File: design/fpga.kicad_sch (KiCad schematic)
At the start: 80 parts, among them J7 DEBUG_FPGA_GPIO, J8 DIGILENT_JTAG_HS2_01X06, SW1 RST, SW2 PROG, U13 XC7S15-FTGB196, U14 IS25LP064A-JKx

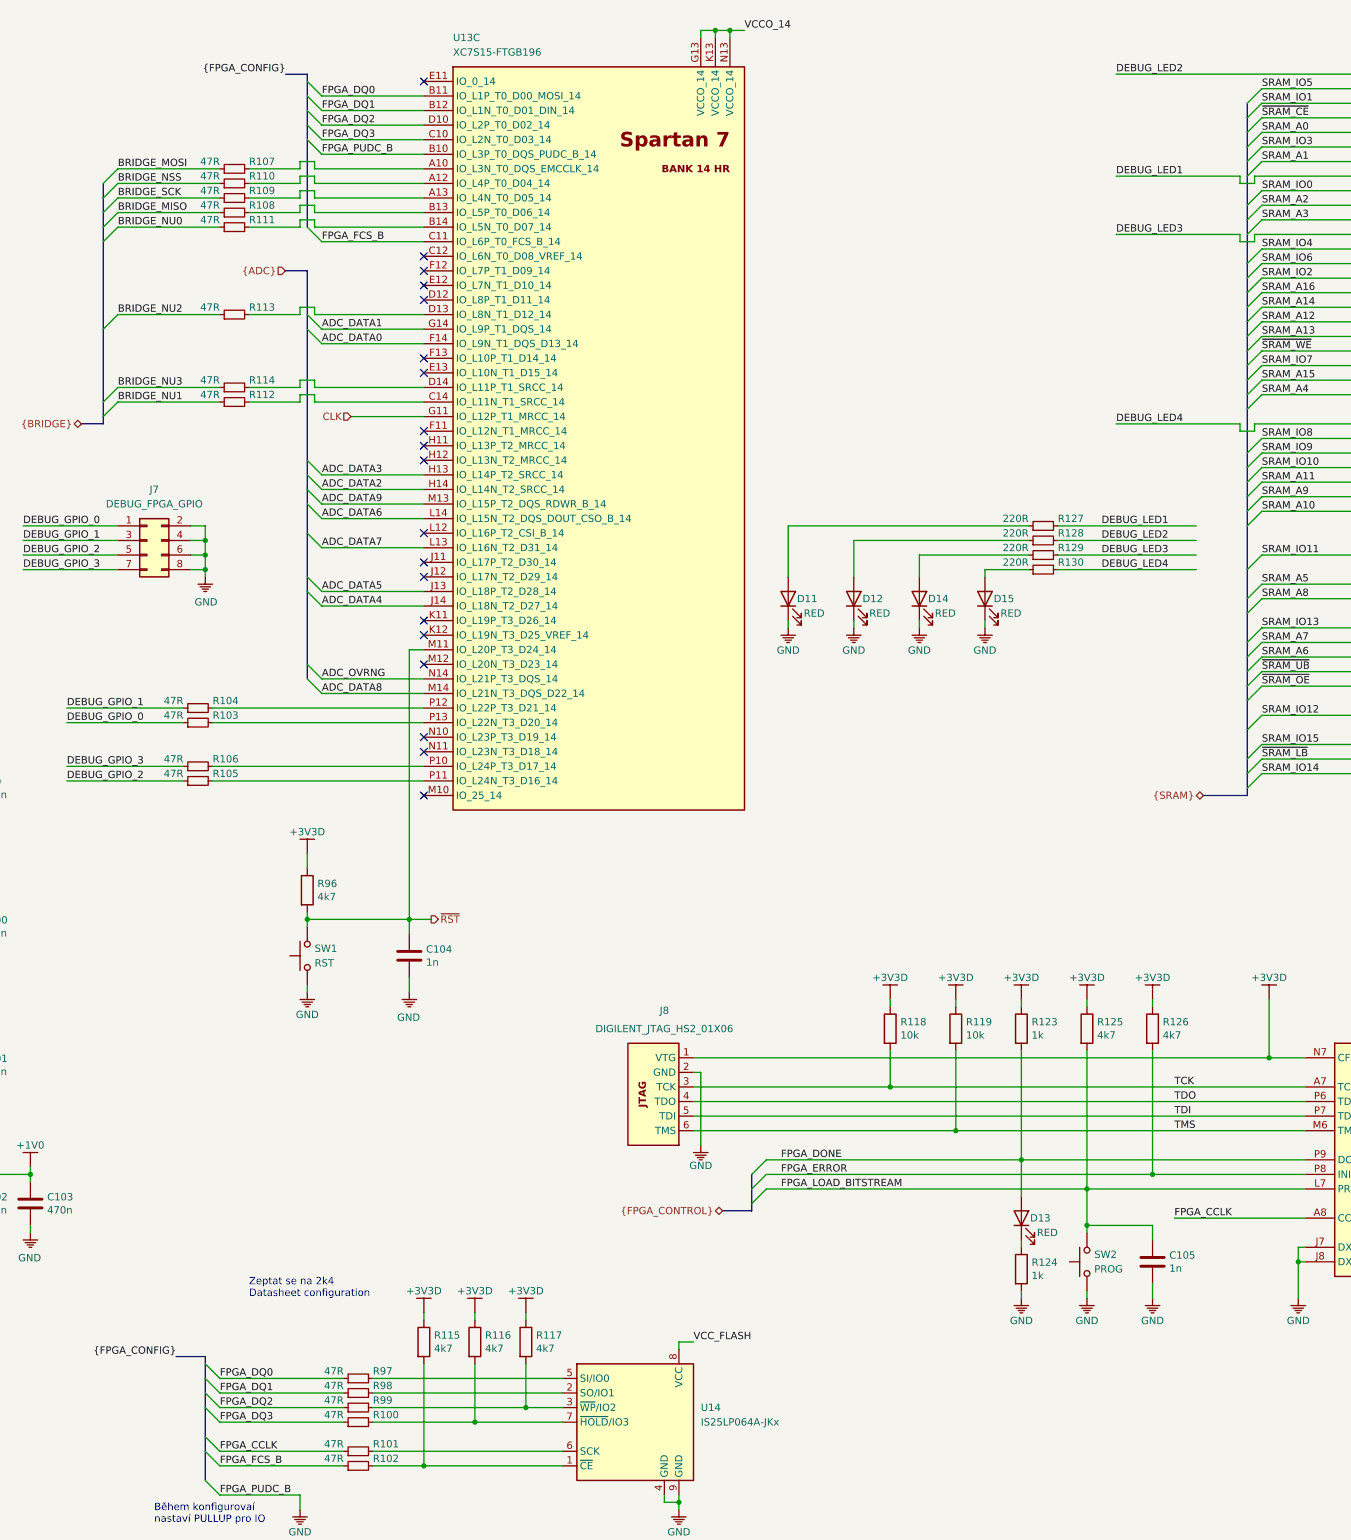
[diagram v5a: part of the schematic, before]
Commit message: Added FTDI RST support
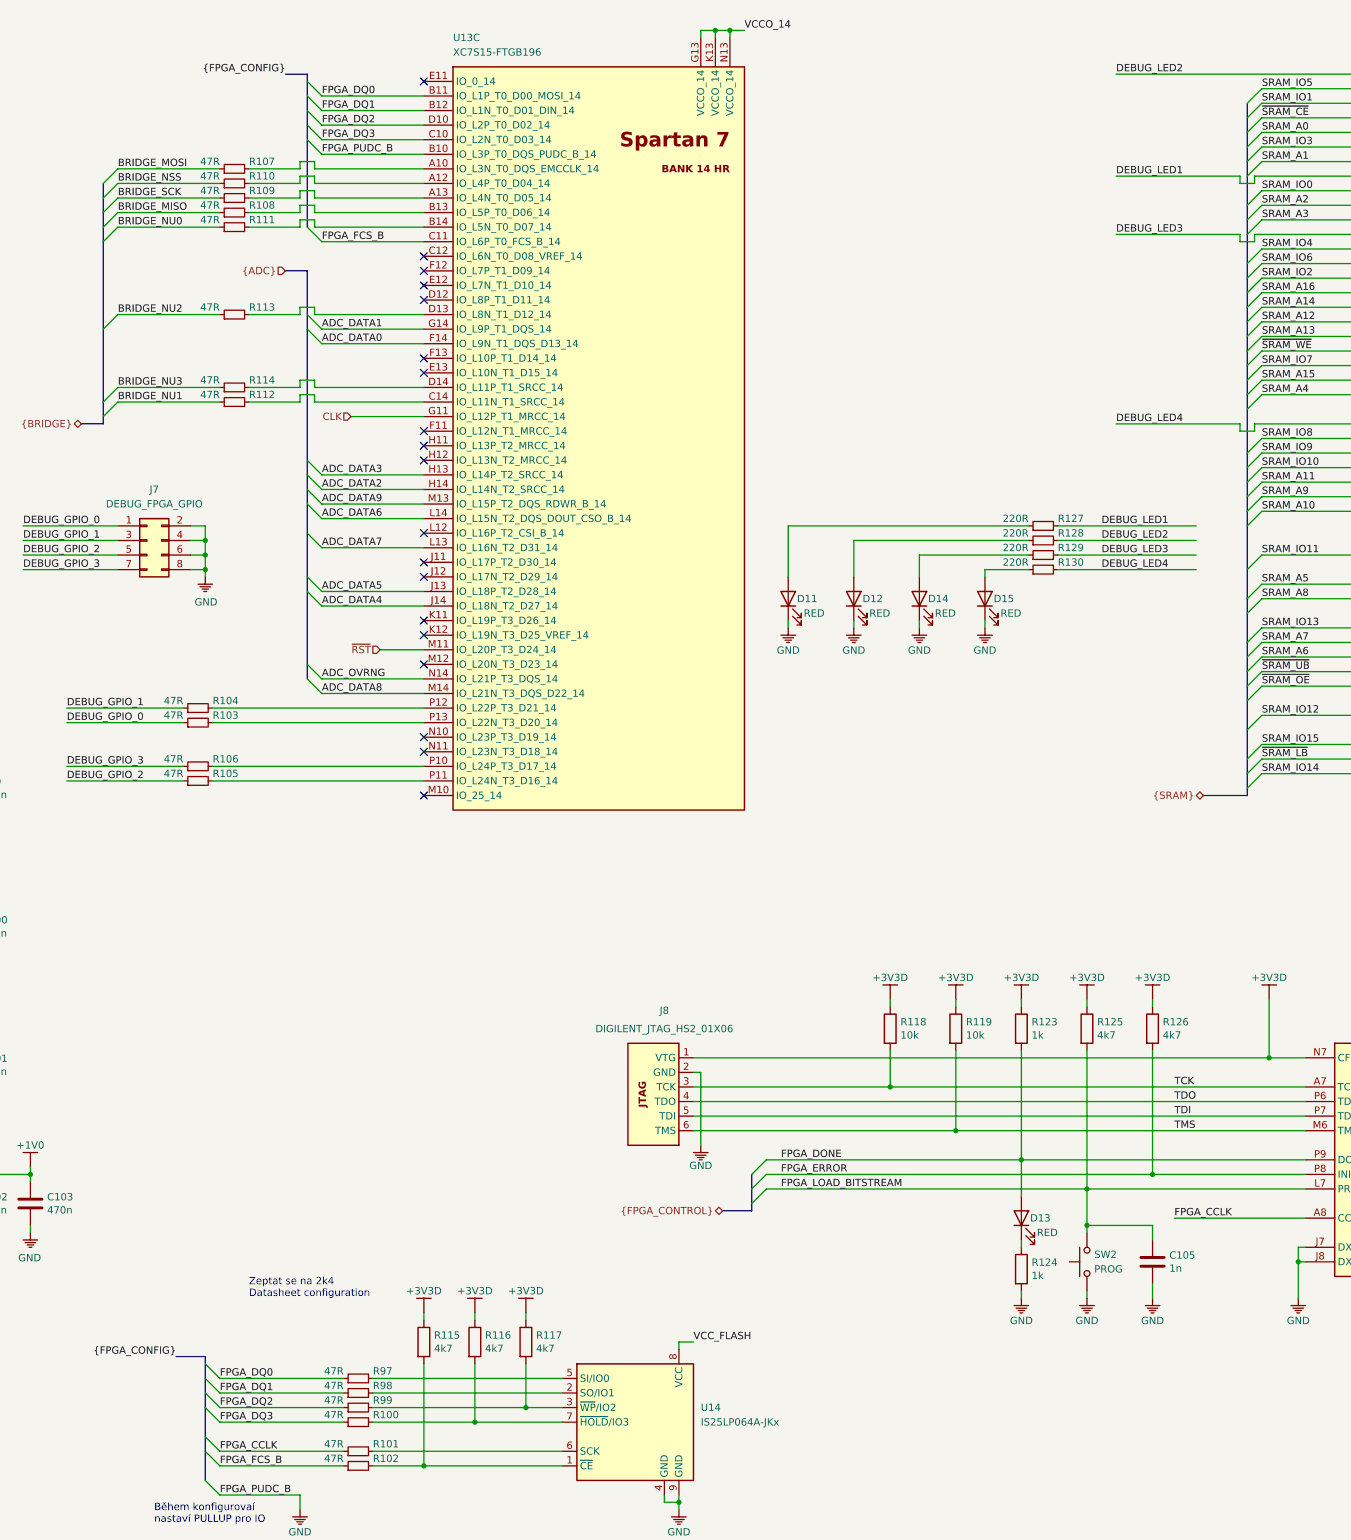
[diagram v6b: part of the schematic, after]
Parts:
- removed C104: 1n, Capacitor_SMD:C_0402_1005Metric, symbol Device:C
- removed R96: 4k7, Resistor_SMD:R_0603_1608Metric, symbol Device:R
- removed SW1: RST, Button_Switch_SMD:SW_SPST_CK_RS282G05A3, symbol Switch:SW_Push

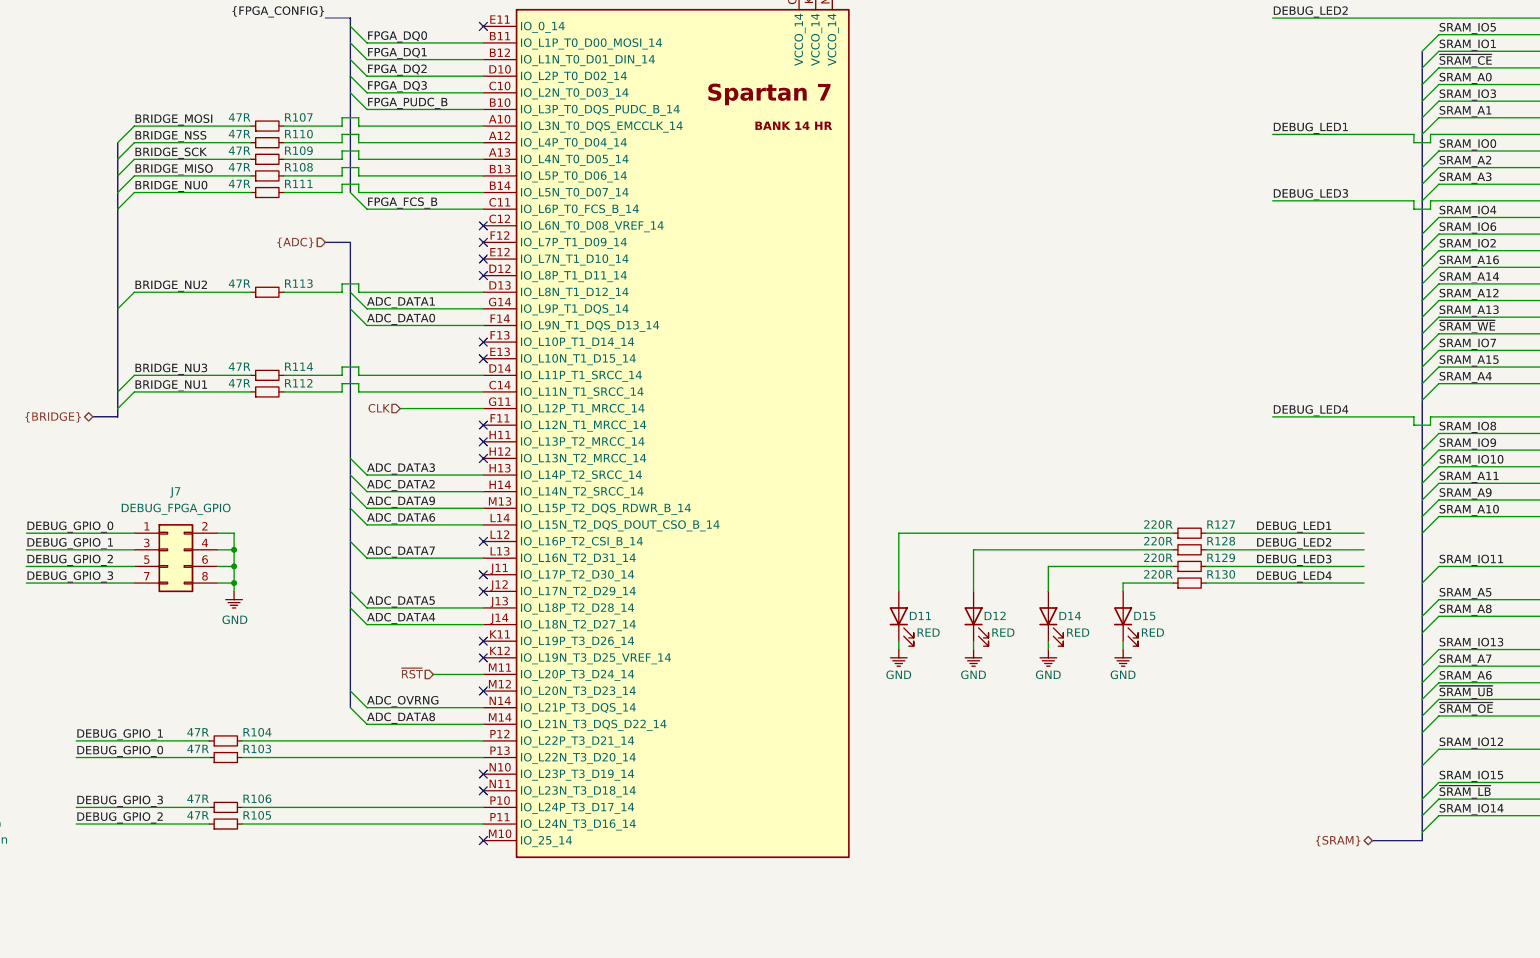
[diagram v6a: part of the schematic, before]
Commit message: Fixed MCU RST
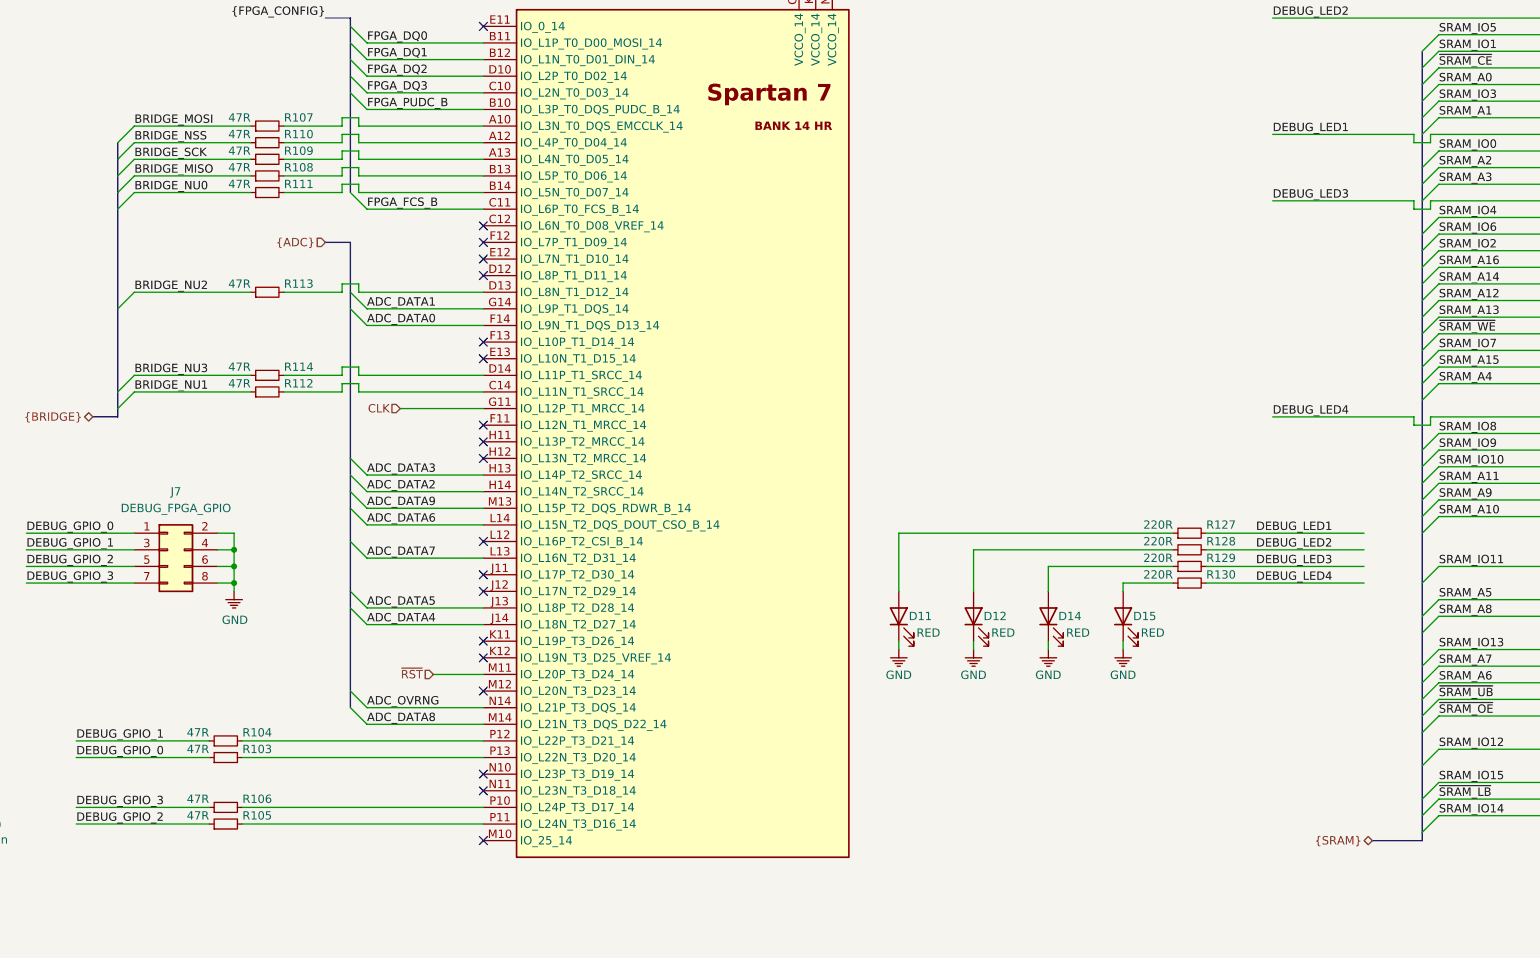
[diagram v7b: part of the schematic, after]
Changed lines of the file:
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@@
 (kicad_sch (version 20200512) (host eeschema "5.99.0-unknown-d72a778~101~ubuntu18.04.1")
-  (page 8 8)
+  (page 1 8)
   (paper "A3")
   (title_block
@@
     (company "Jan Vykydal")
   )
+  (bus_alias "BRIDGE" (members "BRIDGE_MOSI" "BRIDGE_MISO" "BRIDGE_SCK" "BRIDGE_NSS" "BRIDGE_NU[0..3]"))
   (bus_alias "FPGA_CONTROL" (members "FPGA_DONE" "FPGA_ERROR" "FPGA_LOAD_BITSTREAM"))
   (bus_alias "FPGA_CONFIG" (members "FPGA_DQ[0..3]" "FPGA_CCLK" "FPGA_FCS_B" "FPGA_PUDC_B"))
-  (bus_alias "BRIDGE" (members "BRIDGE_MOSI" "BRIDGE_MISO" "BRIDGE_SCK" "BRIDGE_NSS" "BRIDGE_NU[0..3]"))
   (junction (at 26.67 26.67))
   (junction (at 26.67 29.21))
@@
   (junction (at 391.16 232.41))
   (junction (at 392.43 16.51))
+  (no_connect (at 175.26 87.63))
+  (no_connect (at 175.26 77.47))
+  (no_connect (at 175.26 92.71))
+  (no_connect (at 175.26 151.13))
+  (no_connect (at 175.26 90.17))
+  (no_connect (at 175.26 57.15))
+  (no_connect (at 175.26 110.49))
   (no_connect (at 339.09 111.76))
+  (no_connect (at 339.09 134.62))
+  (no_connect (at 175.26 128.27))
+  (no_connect (at 175.26 120.65))
+  (no_connect (at 175.26 62.23))
   (no_connect (at 175.26 64.77))
-  (no_connect (at 175.26 128.27))
+  (no_connect (at 175.26 143.51))
+  (no_connect (at 339.09 106.68))
+  (no_connect (at 175.26 59.69))
+  (no_connect (at 175.26 26.67))
+  (no_connect (at 175.26 113.03))
+  (no_connect (at 339.09 83.82))
+  (no_connect (at 175.26 105.41))
   (no_connect (at 339.09 149.86))
-  (no_connect (at 175.26 90.17))
+  (no_connect (at 339.09 104.14))
+  (no_connect (at 175.26 140.97))
+  (no_connect (at 175.26 74.93))
   (no_connect (at 175.26 123.19))
-  (no_connect (at 175.26 143.51))
-  (no_connect (at 175.26 59.69))
-  (no_connect (at 339.09 104.14))
-  (no_connect (at 175.26 77.47))
-  (no_connect (at 339.09 83.82))
   (no_connect (at 339.09 119.38))
-  (no_connect (at 175.26 151.13))
-  (no_connect (at 175.26 92.71))
-  (no_connect (at 175.26 87.63))
-  (no_connect (at 339.09 106.68))
-  (no_connect (at 339.09 134.62))
   (no_connect (at 339.09 139.7))
-  (no_connect (at 175.26 74.93))
-  (no_connect (at 175.26 26.67))
-  (no_connect (at 175.26 120.65))
-  (no_connect (at 175.26 105.41))
-  (no_connect (at 175.26 62.23))
-  (no_connect (at 175.26 110.49))
-  (no_connect (at 175.26 57.15))
-  (no_connect (at 175.26 140.97))
-  (no_connect (at 175.26 113.03))
   (bus_entry (at 119.38 44.45) (size 2.54 -2.54))
   (bus_entry (at 119.38 46.99) (size 2.54 -2.54))
@@
   (wire (pts (xy 392.43 16.51) (xy 394.97 16.51)))
   (bus (pts (xy 115.57 86.36) (xy 119.38 86.36)))
-  (bus (pts (xy 119.38 44.45) (xy 119.38 49.53)))
-  (bus (pts (xy 119.38 49.53) (xy 119.38 54.61)))
-  (bus (pts (xy 119.38 54.61) (xy 119.38 82.55)))
-  (bus (pts (xy 119.38 82.55) (xy 119.38 86.36)))
+  (bus (pts (xy 119.38 44.45) (xy 119.38 46.99)))
+  (bus (pts (xy 119.38 46.99) (xy 119.38 52.07)))
+  (bus (pts (xy 119.38 52.07) (xy 119.38 69.85)))
+  (bus (pts (xy 119.38 69.85) (xy 119.38 85.09)))
+  (bus (pts (xy 119.38 85.09) (xy 119.38 86.36)))
   (bus (pts (xy 132.08 248.92) (xy 137.16 248.92)))
   (bus (pts (xy 137.16 248.92) (xy 137.16 252.73)))
@@
   (bus (pts (xy 154.94 29.21) (xy 154.94 34.29)))
   (bus (pts (xy 154.94 34.29) (xy 154.94 52.07)))
-  (bus (pts (xy 154.94 59.69) (xy 154.94 69.85)))
-  (bus (pts (xy 154.94 69.85) (xy 154.94 95.25)))
-  (bus (pts (xy 154.94 95.25) (xy 154.94 100.33)))
+  (bus (pts (xy 154.94 59.69) (xy 154.94 67.31)))
+  (bus (pts (xy 154.94 67.31) (xy 154.94 92.71)))
+  (bus (pts (xy 154.94 92.71) (xy 154.94 97.79)))
+  (bus (pts (xy 154.94 97.79) (xy 154.94 100.33)))
   (bus (pts (xy 154.94 100.33) (xy 154.94 113.03)))
   (bus (pts (xy 154.94 113.03) (xy 154.94 128.27)))
@@
   (bus (pts (xy 318.77 30.48) (xy 318.77 35.56)))
   (bus (pts (xy 318.77 35.56) (xy 318.77 40.64)))
-  (bus (pts (xy 318.77 40.64) (xy 318.77 43.18)))
-  (bus (pts (xy 318.77 43.18) (xy 318.77 50.8)))
-  (bus (pts (xy 318.77 50.8) (xy 318.77 53.34)))
+  (bus (pts (xy 318.77 40.64) (xy 318.77 48.26)))
+  (bus (pts (xy 318.77 48.26) (xy 318.77 53.34)))
   (bus (pts (xy 318.77 53.34) (xy 318.77 60.96)))
   (bus (pts (xy 318.77 60.96) (xy 318.77 66.04)))
-  (bus (pts (xy 318.77 66.04) (xy 318.77 68.58)))
-  (bus (pts (xy 318.77 68.58) (xy 318.77 73.66)))
-  (bus (pts (xy 318.77 73.66) (xy 318.77 76.2)))
-  (bus (pts (xy 318.77 76.2) (xy 318.77 81.28)))
+  (bus (pts (xy 318.77 66.04) (xy 318.77 71.12)))
+  (bus (pts (xy 318.77 71.12) (xy 318.77 73.66)))
+  (bus (pts (xy 318.77 73.66) (xy 318.77 78.74)))
+  (bus (pts (xy 318.77 78.74) (xy 318.77 81.28)))
   (bus (pts (xy 318.77 81.28) (xy 318.77 91.44)))
   (bus (pts (xy 318.77 91.44) (xy 318.77 96.52)))
   (bus (pts (xy 318.77 96.52) (xy 318.77 101.6)))
-  (bus (pts (xy 318.77 101.6) (xy 318.77 104.14)))
-  (bus (pts (xy 318.77 104.14) (xy 318.77 116.84)))
-  (bus (pts (xy 318.77 116.84) (xy 318.77 124.46)))
-  (bus (pts (xy 318.77 124.46) (xy 318.77 129.54)))
-  (bus (pts (xy 318.77 129.54) (xy 318.77 132.08)))
-  (bus (pts (xy 318.77 132.08) (xy 318.77 139.7)))
-  (bus (pts (xy 318.77 139.7) (xy 318.77 147.32)))
-  (bus (pts (xy 318.77 147.32) (xy 318.77 151.13)))
+  (bus (pts (xy 318.77 101.6) (xy 318.77 111.76)))
+  (bus (pts (xy 318.77 111.76) (xy 318.77 119.38)))
+  (bus (pts (xy 318.77 119.38) (xy 318.77 127)))
+  (bus (pts (xy 318.77 127) (xy 318.77 129.54)))
+  (bus (pts (xy 318.77 129.54) (xy 318.77 134.62)))
+  (bus (pts (xy 318.77 134.62) (xy 318.77 144.78)))
+  (bus (pts (xy 318.77 144.78) (xy 318.77 149.86)))
+  (bus (pts (xy 318.77 149.86) (xy 318.77 151.13)))
   (bus (pts (xy 318.77 151.13) (xy 311.15 151.13)))
   (text "Během konfigurovaí\nnastaví PULLUP pro IO" (at 128.27 278.13 0)

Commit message: Updated some layout
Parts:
- renumbered C96 to C100, C97 to C101, C98 to C102, C99 to C103, C100 to C104, C101 to C105, C102 to C106, C103 to C107, C105 to C108, C69 to C73, C70 to C74, C71 to C75, C72 to C76, C73 to C77, C74 to C78, C75 to C79, C76 to C80, C77 to C81, C78 to C82, C79 to C83, C80 to C84, C81 to C85, C82 to C86, C83 to C87, C84 to C88, C85 to C89, C86 to C90, C87 to C91, C88 to C92, C89 to C93, C90 to C94, C91 to C95, C92 to C96, C93 to C97, C94 to C98, C95 to C99, D14 to D13, D15 to D14, D13 to D15, R103 to R100, R106 to R101, R105 to R102, R107 to R103, R110 to R104, R109 to R105, R108 to R106, R111 to R107, R113 to R108, R114 to R109, R112 to R110, R97 to R111, R98 to R112, R99 to R113, R100 to R114, R101 to R115, R102 to R116, R115 to R117, R116 to R118, R117 to R119, R118 to R120, R119 to R121, R123 to R122, R124 to R123, R127 to R124, R128 to R125, R129 to R126, R130 to R127, R125 to R128, R126 to R129, R104 to R99, U13 to U14, U14 to U15
